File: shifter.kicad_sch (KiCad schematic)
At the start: 11 parts

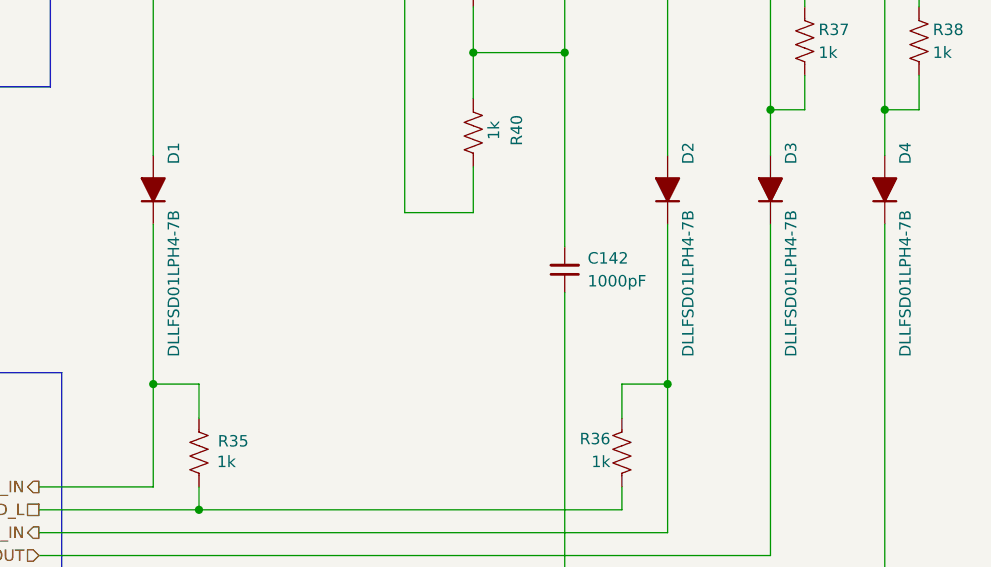
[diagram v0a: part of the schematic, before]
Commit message: changed all the level shifting diodes to SOD-523 packages for #6
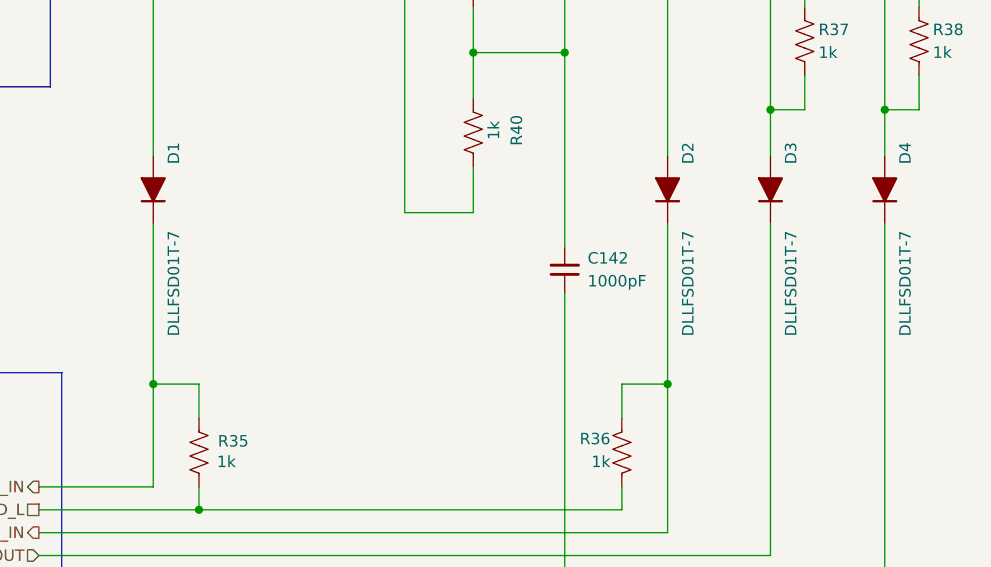
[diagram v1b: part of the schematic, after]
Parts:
- D1, D2, D3, D4: value DLLFSD01LPH4-7B -> DLLFSD01T-7; footprint bitaxe:DIODE_DLLFSD01LPH4-7B_DIO -> bitaxe:D_SOD-523; DK 31-DLLFSD01LPH4-7BCT-ND -> DLLFSD01T-7DICT-ND; PARTNO DLLFSD01LPH4-7B -> DLLFSD01T-7
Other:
- title: (none) -> Bitaxe Intel Reference Design System
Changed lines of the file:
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@@
 	(paper "A4")
 	(title_block
-		(date "2025-10-01")
-		(rev "1300xx")
+		(title "Bitaxe Intel Reference Design System")
+		(date "2026-02-09")
+		(rev "1300xxx")
 	)
 	(rectangle
@@
 			)
 		)
-		(property "Value" "DLLFSD01LPH4-7B"
+		(property "Value" "DLLFSD01T-7"
 			(at 177.546 94.234 0)
 			(effects
@@
 			)
 		)
-		(property "Footprint" "bitaxe:DIODE_DLLFSD01LPH4-7B_DIO"
+		(property "Footprint" "bitaxe:D_SOD-523"
 			(at 170.18 83.82 0)
 			(effects
@@
 			)
 		)
-		(property "DK" "31-DLLFSD01LPH4-7BCT-ND"
+		(property "DK" "DLLFSD01T-7DICT-ND"
 			(at 172.212 83.312 0)
 			(effects
@@
 			)
 		)
-		(property "PARTNO" "DLLFSD01LPH4-7B"
+		(property "PARTNO" "DLLFSD01T-7"
 			(at 168.402 84.074 0)
 			(effects
@@
 			)
 		)
-		(property "Value" "DLLFSD01LPH4-7B"
+		(property "Value" "DLLFSD01T-7"
 			(at 96.266 94.234 0)
 			(effects
@@
 			)
 		)
-		(property "Footprint" "bitaxe:DIODE_DLLFSD01LPH4-7B_DIO"
+		(property "Footprint" "bitaxe:D_SOD-523"
 			(at 88.9 83.82 0)
 			(effects
@@
 			)
 		)
-		(property "DK" "31-DLLFSD01LPH4-7BCT-ND"
+		(property "DK" "DLLFSD01T-7DICT-ND"
 			(at 90.932 83.312 0)
 			(effects
@@
 			)
 		)
-		(property "PARTNO" "DLLFSD01LPH4-7B"
+		(property "PARTNO" "DLLFSD01T-7"
 			(at 87.122 84.074 0)
 			(effects
@@
 			)
 		)
-		(property "Value" "DLLFSD01LPH4-7B"
+		(property "Value" "DLLFSD01T-7"
 			(at 164.846 94.234 0)
 			(effects
@@
 			)
 		)
-		(property "Footprint" "bitaxe:DIODE_DLLFSD01LPH4-7B_DIO"
+		(property "Footprint" "bitaxe:D_SOD-523"
 			(at 157.48 83.82 0)
 			(effects
@@
 			)
 		)
-		(property "DK" "31-DLLFSD01LPH4-7BCT-ND"
+		(property "DK" "DLLFSD01T-7DICT-ND"
 			(at 159.512 83.312 0)
 			(effects
@@
 			)
 		)
-		(property "PARTNO" "DLLFSD01LPH4-7B"
+		(property "PARTNO" "DLLFSD01T-7"
 			(at 155.702 84.074 0)
 			(effects
@@
 			)
 		)
-		(property "Value" "DLLFSD01LPH4-7B"
+		(property "Value" "DLLFSD01T-7"
 			(at 153.416 94.234 0)
 			(effects
@@
 			)
 		)
-		(property "Footprint" "bitaxe:DIODE_DLLFSD01LPH4-7B_DIO"
+		(property "Footprint" "bitaxe:D_SOD-523"
 			(at 146.05 83.82 0)
 			(effects
@@
 			)
 		)
-		(property "DK" "31-DLLFSD01LPH4-7BCT-ND"
+		(property "DK" "DLLFSD01T-7DICT-ND"
 			(at 148.082 83.312 0)
 			(effects
@@
 			)
 		)
-		(property "PARTNO" "DLLFSD01LPH4-7B"
+		(property "PARTNO" "DLLFSD01T-7"
 			(at 144.272 84.074 0)
 			(effects
